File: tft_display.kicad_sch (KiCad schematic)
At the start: 8 parts, among them J5 Conn_01x04_Socket, J6 Conn_01x08_Socket, J8 Conn_01x06_Socket, Q3 AO3401A

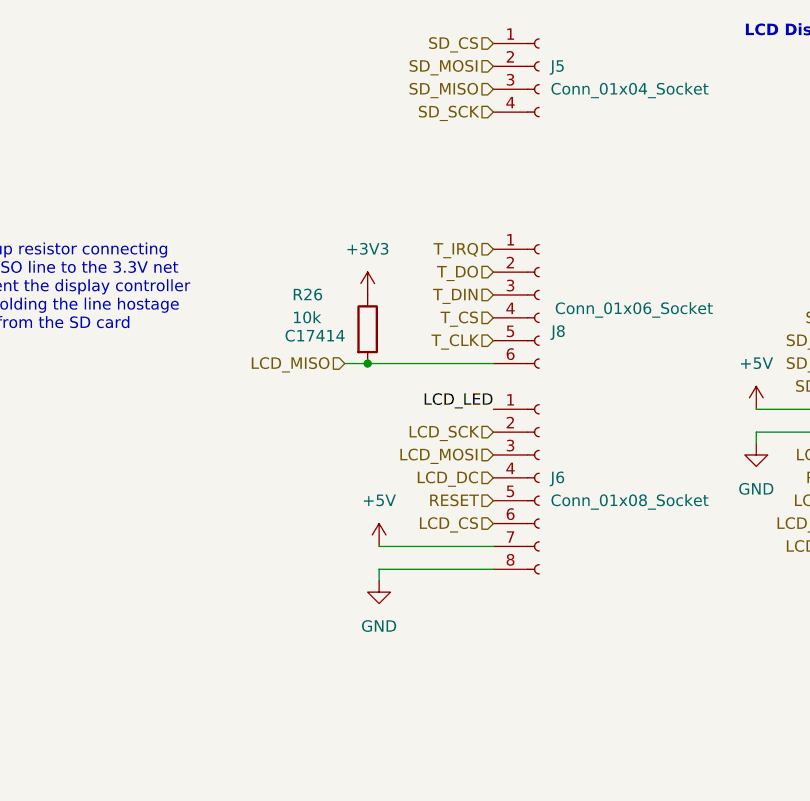
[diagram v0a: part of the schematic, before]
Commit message: swapped around TFT pinout to match physical board
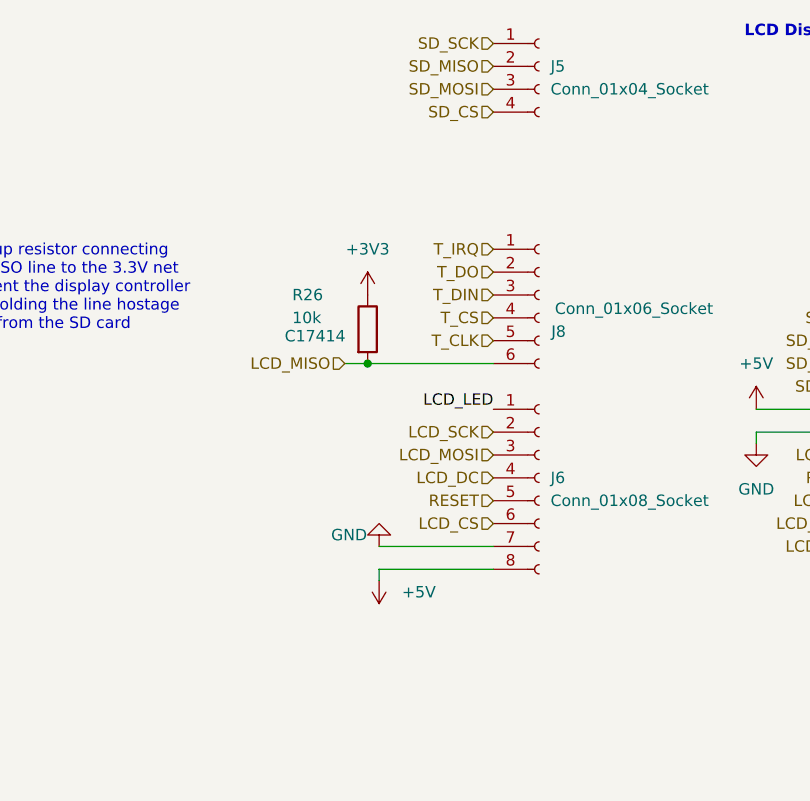
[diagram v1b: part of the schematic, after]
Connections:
- net +5V: now also J6.8 (Pin_8); no longer J6.7 (Pin_7)
- net GND: now also J6.7 (Pin_7); no longer J6.8 (Pin_8)
- net SD_CS: now also J5.4 (Pin_4); no longer J5.1 (Pin_1)
- net SD_MISO: now also J5.2 (Pin_2); no longer J5.3 (Pin_3)
- net SD_MOSI: now also J5.3 (Pin_3); no longer J5.2 (Pin_2)
- net SD_SCK: now also J5.1 (Pin_1); no longer J5.4 (Pin_4)
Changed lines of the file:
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@@
 	(hierarchical_label "SD_SCK"
 		(shape input)
-		(at 101.6 46.99 180)
+		(at 101.6 39.37 180)
 		(effects
 			(font
@@
 	(hierarchical_label "SD_MOSI"
 		(shape input)
-		(at 101.6 41.91 180)
+		(at 101.6 44.45 180)
 		(effects
 			(font
@@
 	(hierarchical_label "SD_MISO"
 		(shape input)
-		(at 101.6 44.45 180)
+		(at 101.6 41.91 180)
 		(effects
 			(font
@@
 	(hierarchical_label "SD_CS"
 		(shape input)
-		(at 101.6 39.37 180)
+		(at 101.6 46.99 180)
 		(effects
 			(font
@@
 	(symbol
 		(lib_id "power:GND")
-		(at 88.9 99.06 0)
+		(at 88.9 95.25 180)
 		(unit 1)
 		(body_style 1)
@@
 		(in_pos_files yes)
 		(dnp no)
-		(fields_autoplaced yes)
 		(property "Reference" "#PWR010"
-			(at 88.9 105.41 0)
+			(at 88.9 88.9 0)
 			(hide yes)
 			(show_name no)
@@
 		)
 		(property "Value" "GND"
-			(at 88.9 104.14 0)
+			(at 83.566 93.98 0)
 			(show_name no)
 			(do_not_autoplace no)
@@
 					(size 1.27 1.27)
 				)
+				(justify right)
 			)
 		)
 		(property "Footprint" ""
-			(at 88.9 99.06 0)
+			(at 88.9 95.25 0)
 			(hide yes)
 			(show_name no)
@@
 		)
 		(property "Datasheet" ""
-			(at 88.9 99.06 0)
+			(at 88.9 95.25 0)
 			(hide yes)
 			(show_name no)
@@
 		)
 		(property "Description" "Power symbol creates a global label with name \"GND\" , ground"
-			(at 88.9 99.06 0)
+			(at 88.9 95.25 0)
 			(hide yes)
 			(show_name no)
@@
 	(symbol
 		(lib_id "power:+5V")
-		(at 88.9 95.25 0)
+		(at 88.9 99.06 180)
 		(unit 1)
 		(body_style 1)
@@
 		(fields_autoplaced yes)
 		(property "Reference" "#PWR02"
-			(at 88.9 99.06 0)
+			(at 88.9 95.25 0)
 			(hide yes)
 			(show_name no)
@@
 		)
 		(property "Value" "+5V"
-			(at 88.9 90.17 0)
+			(at 91.44 100.3299 0)
 			(show_name no)
 			(do_not_autoplace no)
@@
 					(size 1.27 1.27)
 				)
+				(justify right)
 			)
 		)
 		(property "Footprint" ""
-			(at 88.9 95.25 0)
+			(at 88.9 99.06 0)
 			(hide yes)
 			(show_name no)
@@
 		)
 		(property "Datasheet" ""
-			(at 88.9 95.25 0)
+			(at 88.9 99.06 0)
 			(hide yes)
 			(show_name no)
@@
 		)
 		(property "Description" "Power symbol creates a global label with name \"+5V\""
-			(at 88.9 95.25 0)
+			(at 88.9 99.06 0)
 			(hide yes)
 			(show_name no)

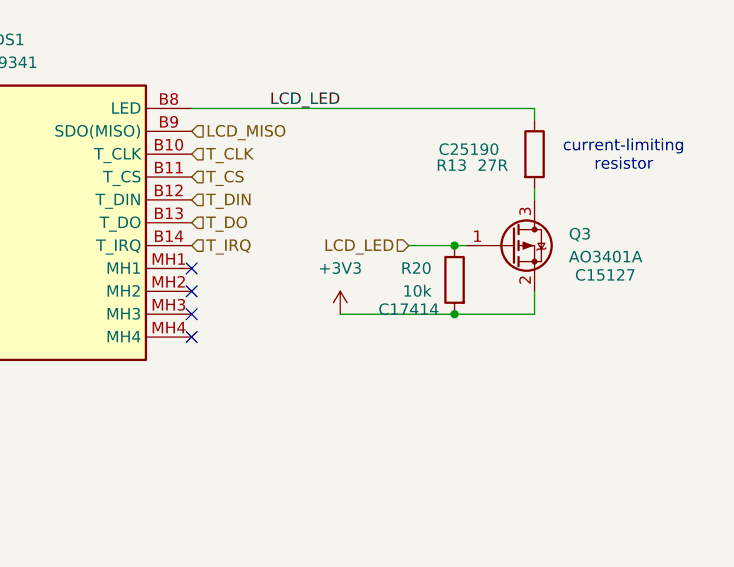
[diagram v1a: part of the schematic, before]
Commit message: add 100ohm current limit resistor to TFT LED GPIO control pin
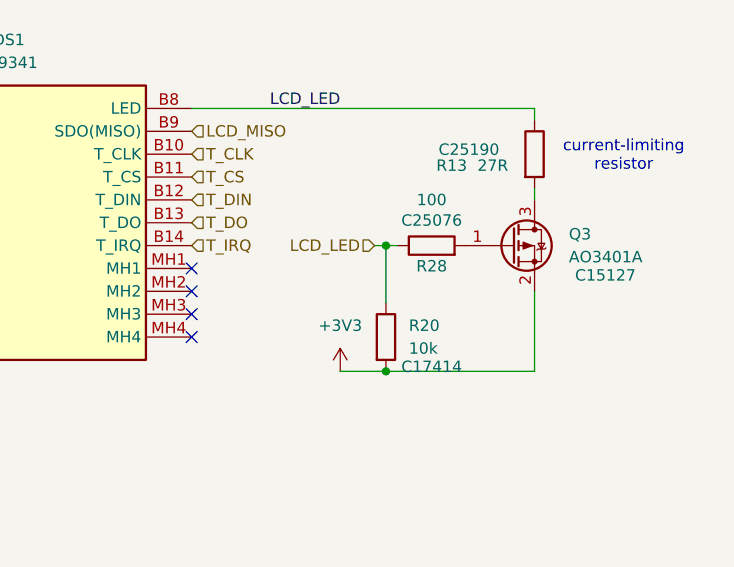
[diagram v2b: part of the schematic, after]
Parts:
- added R28: 100, Resistor_SMD:R_0402_1005Metric, symbol Device:R
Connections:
- net LCD_LED: now also R28.1; no longer Q3.1 (G)
- new net: Q3.1 (G), R28.2
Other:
- moved on the sheet: R20

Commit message: Update sheet naming
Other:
- company: (none) -> Alister, Damien, Nils
- title: (none) -> CC3501 Design Project
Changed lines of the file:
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@@
 	(generator_version "10.0")
 	(paper "A4")
+	(title_block
+		(title "CC3501 Design Project")
+		(date "2026-06-22")
+		(rev "1")
+		(company "Alister, Damien, Nils")
+	)
 	(text "LCD Display + Touch + SD Card (SPI)"
 		(exclude_from_sim no)
